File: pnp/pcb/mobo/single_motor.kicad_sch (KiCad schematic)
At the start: 17 parts, among them J27 TMC_PIN_HEADER, M1 Stepper_Motor

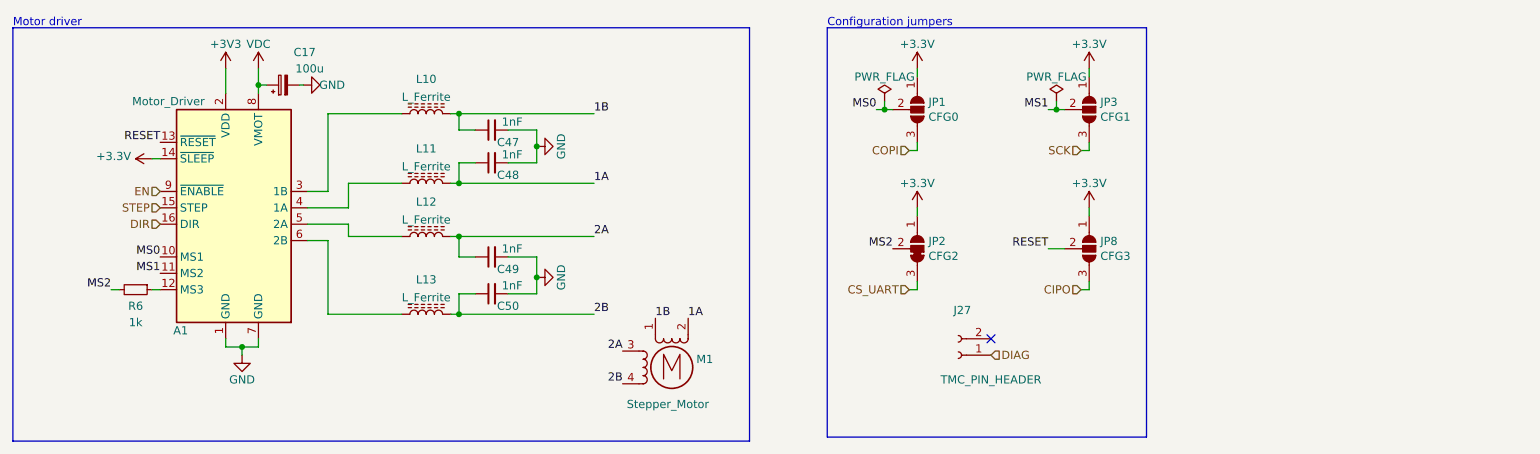
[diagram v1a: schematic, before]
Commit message: Redesign finished
Completed Board redesign and adding more EMC improvements.
Changed all the part numbers to have a Mouser orderable design (except the JST connectors)
All outputs generated
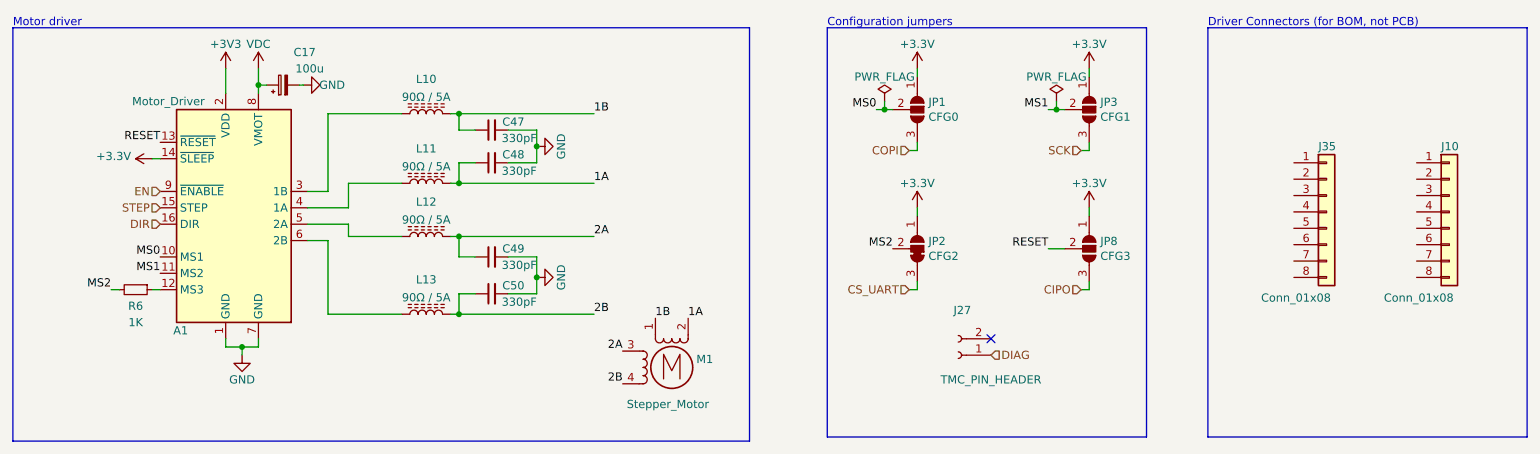
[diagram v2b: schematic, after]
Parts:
- added J10, J35: Conn_01x08, symbol Connector_Generic:Conn_01x08
- C17: Digikey 493-2203-1-ND -> (none); JLCPCB C99837 -> (none); LCSC C3339 -> (none); Mouser 647-UWT1V101MCL1S -> 710-865080545012; Voltage (none) -> 35V
- C47, C48, C49, C50: value 1nF -> 330pF; Mouser (none) -> 80-C0805C331K5RAC; Tolerance (none) -> 10%; Voltage (none) -> 50V
- J27: Mouser (none) -> 571-215297-2
- JP1, JP2, JP3, JP8: Mouser (none) -> -
- L10, L11, L12, L13: value L_Ferrite -> 90Ω / 5A; Mouser (none) -> 70-ILHB0805ER900V
- M1: JLCPCB C37815 -> (none); LCSC C37815 -> (none); Mouser (none) -> Digikey
- R6: value 1k -> 1K; JLCPCB C17513 -> (none); LCSC C17513 -> (none); Mouser (none) -> 756-WCR0805-1K0FI
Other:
- note added: "Driver Connectors (for BOM, not PCB)"
- company: Opulo -> Opulo.io
